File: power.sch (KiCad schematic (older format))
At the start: 30 parts, among them J11 Screw_Terminal_01x02, J2 BATT_OUT, J3 BATT_IN, K1 UMS05-1A80-75L, Q2 Q_NMOS_GSD, Q3 Q_NMOS_GSD, SW2 SW_Reed, U1 TPS3711, U5 P783F-Q24-S5-S

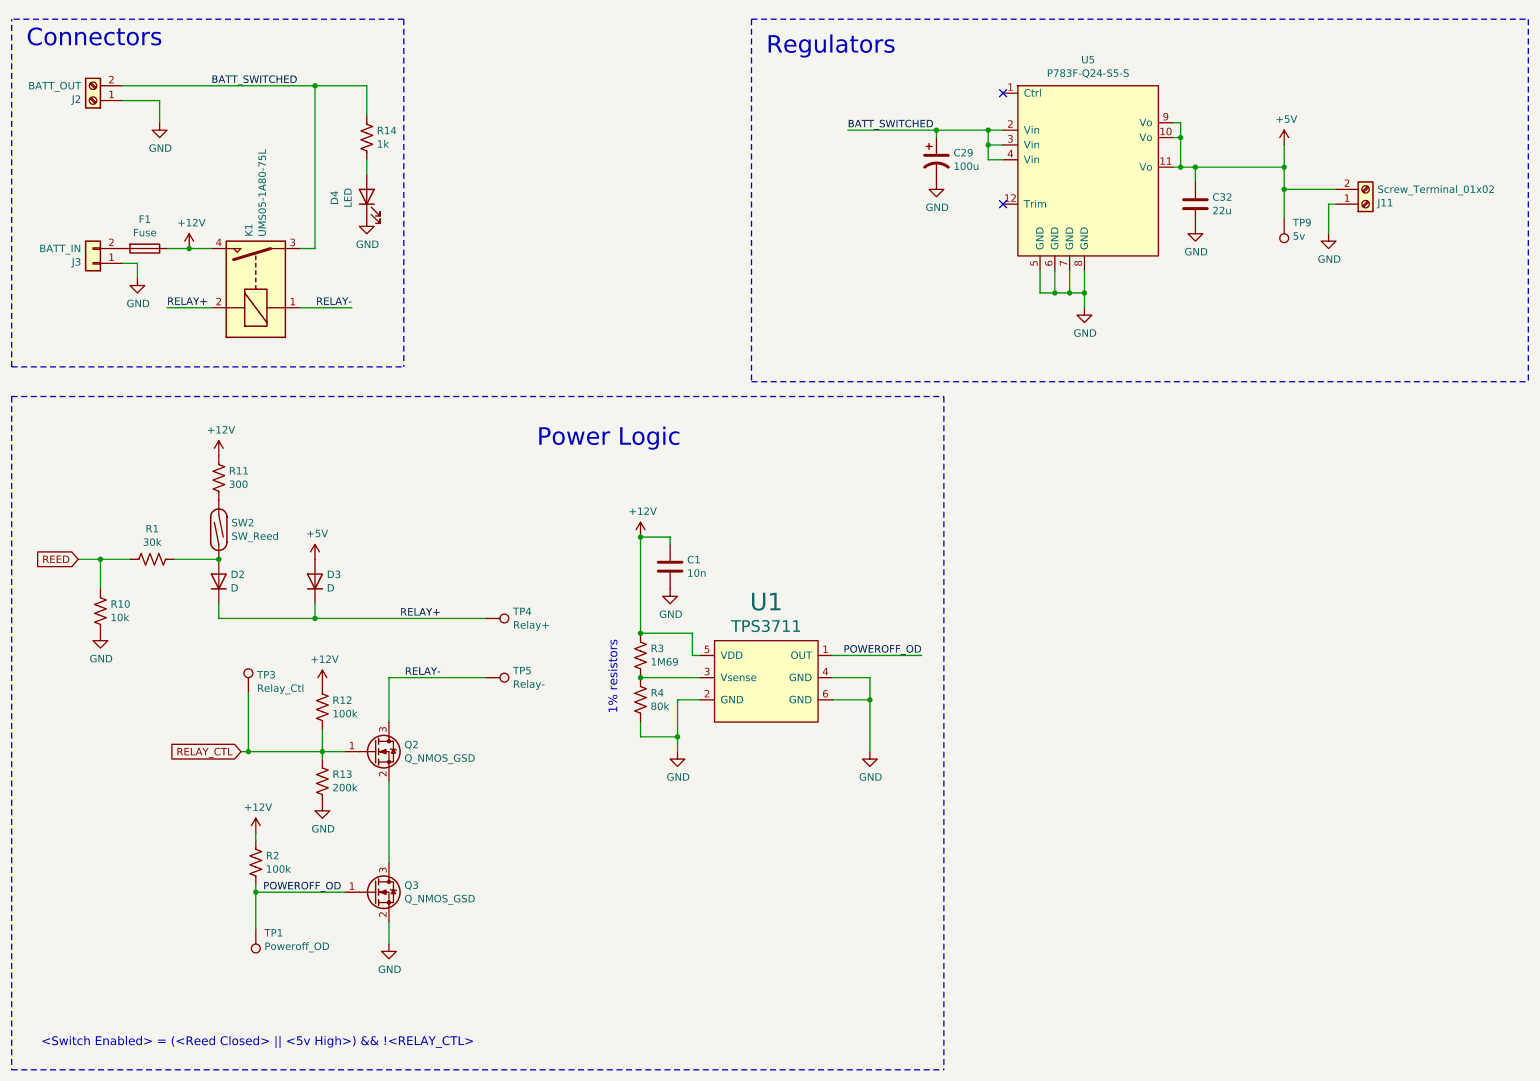
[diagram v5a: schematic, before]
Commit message: Revised for BlueRobotics switch.
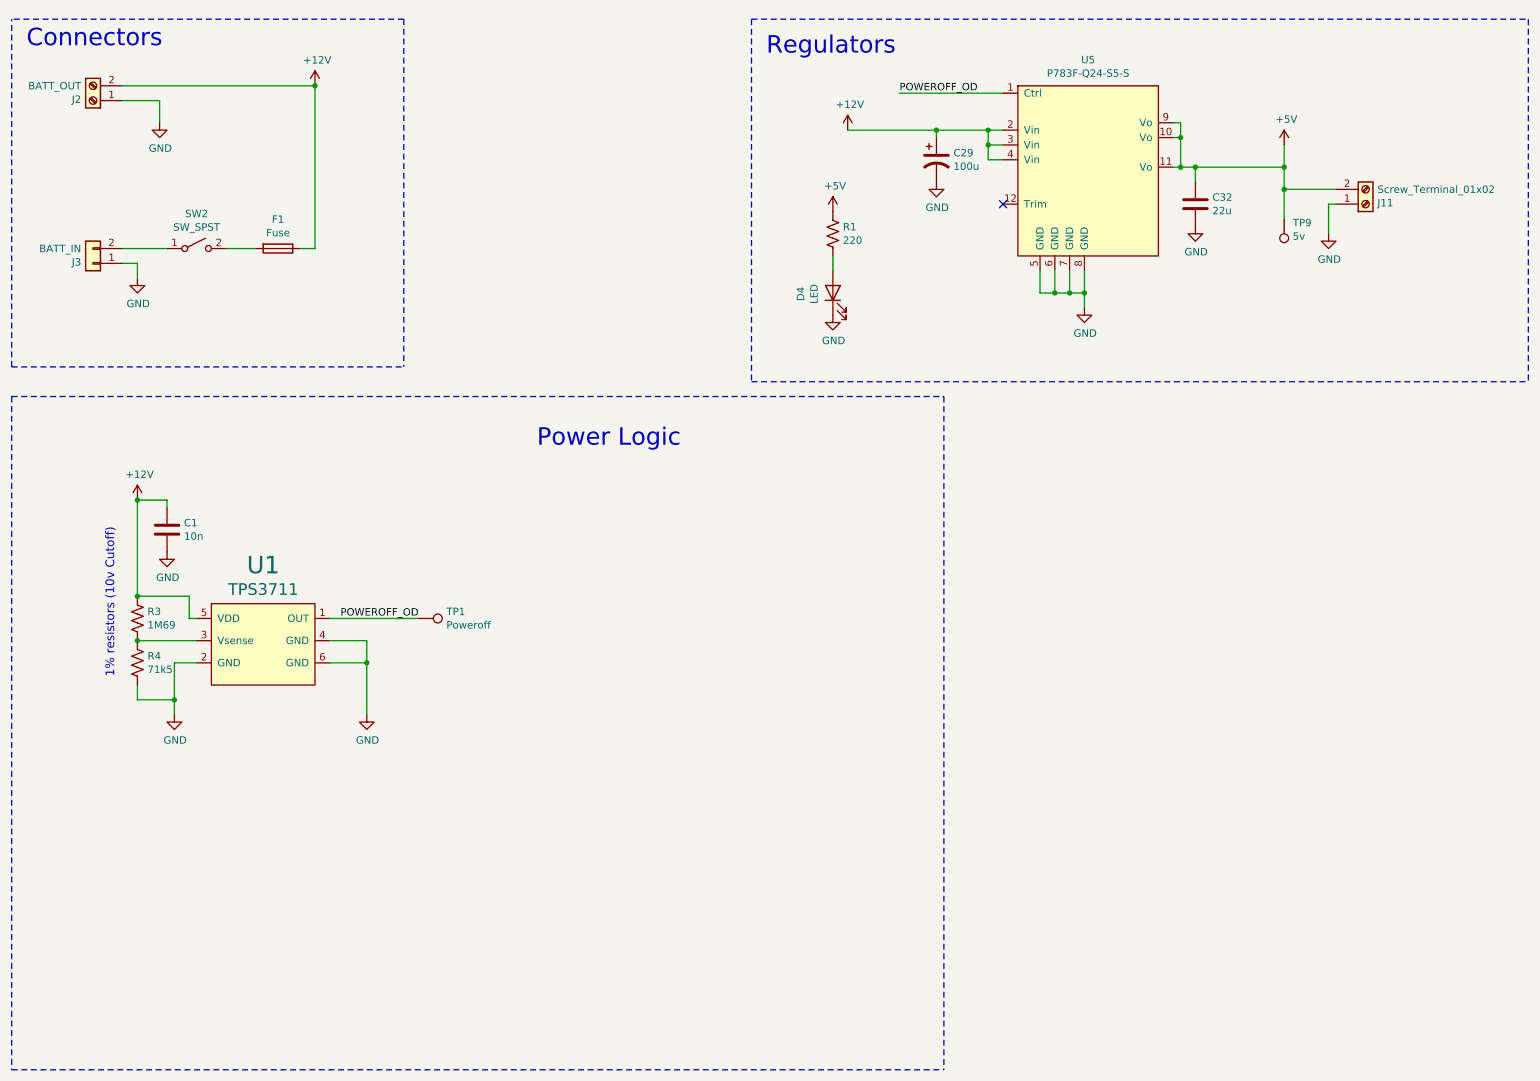
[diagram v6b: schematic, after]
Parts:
- removed D2, D3: D, Diode_SMD:D_1206_3216Metric_Pad1.42x1.75mm_HandSolder, symbol Device:D
- removed K1: UMS05-1A80-75L, Relay_THT:Relay_SPST_TE_PCN-1xxD3MHZ, symbol Relay:UMS05-1A80-75L
- removed Q2, Q3: Q_NMOS_GSD, Package_TO_SOT_SMD:SOT-23_Handsoldering, symbol Device:Q_NMOS_GSD
- removed R10: 10k, Resistor_SMD:R_1206_3216Metric_Pad1.30x1.75mm_HandSolder, symbol Device:R_US
- removed R11: 300, Resistor_SMD:R_1206_3216Metric_Pad1.30x1.75mm_HandSolder, symbol Device:R_US
- removed R12, R2: 100k, Resistor_SMD:R_1206_3216Metric_Pad1.30x1.75mm_HandSolder, symbol Device:R_US
- removed R13: 200k, Resistor_SMD:R_1206_3216Metric_Pad1.30x1.75mm_HandSolder, symbol Device:R_US
- removed R14: 1k, Resistor_SMD:R_1206_3216Metric_Pad1.30x1.75mm_HandSolder, symbol Device:R_US
- removed SW2: SW_Reed, Connector_JST:JST_PH_S2B-PH-K_1x02_P2.00mm_Horizontal, symbol Switch:SW_Reed
- removed TP3: Relay_Ctl, TestPoint:TestPoint_Pad_1.5x1.5mm, symbol Connector:TestPoint
- removed TP4: Relay+, TestPoint:TestPoint_Pad_1.5x1.5mm, symbol Connector:TestPoint
- removed TP5: Relay-, TestPoint:TestPoint_Pad_1.5x1.5mm, symbol Connector:TestPoint
- added SW2: SW_SPST, Connector_JST:JST_XH_S2B-XH-A_1x02_P2.50mm_Horizontal, symbol Switch:SW_SPST
- R1: value 30k -> 220
- R4: value 80k -> 71k5
- TP1: value Poweroff_OD -> Poweroff
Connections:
- net BATT_SWITCHED is gone; now on net +12V: C29.1, J2.2 (Pin_2), U5.2 (Vin), U5.3 (Vin), U5.4 (Vin)
- net REED is gone; now on an unnamed net: R1.2
- net +5V: now also R1.1
- net POWEROFF_OD: now also U5.1 (Ctrl)
- net at J3.2 (Pin_2): now also SW2.1 (A); no longer F1.2
- new net: F1.2, SW2.2 (B)
- no-connect marks 2 -> 1
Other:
- note added: "1% resistors (10v Cutoff)\n"
- note removed: "1% resistors\n"
- note removed: "<Switch Enabled> = (<Reed Closed> || <5v High>) && !<RELAY_CTL>"
- moved on the sheet: C1, D4, F1, R3, R4, U1

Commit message: Added load switch
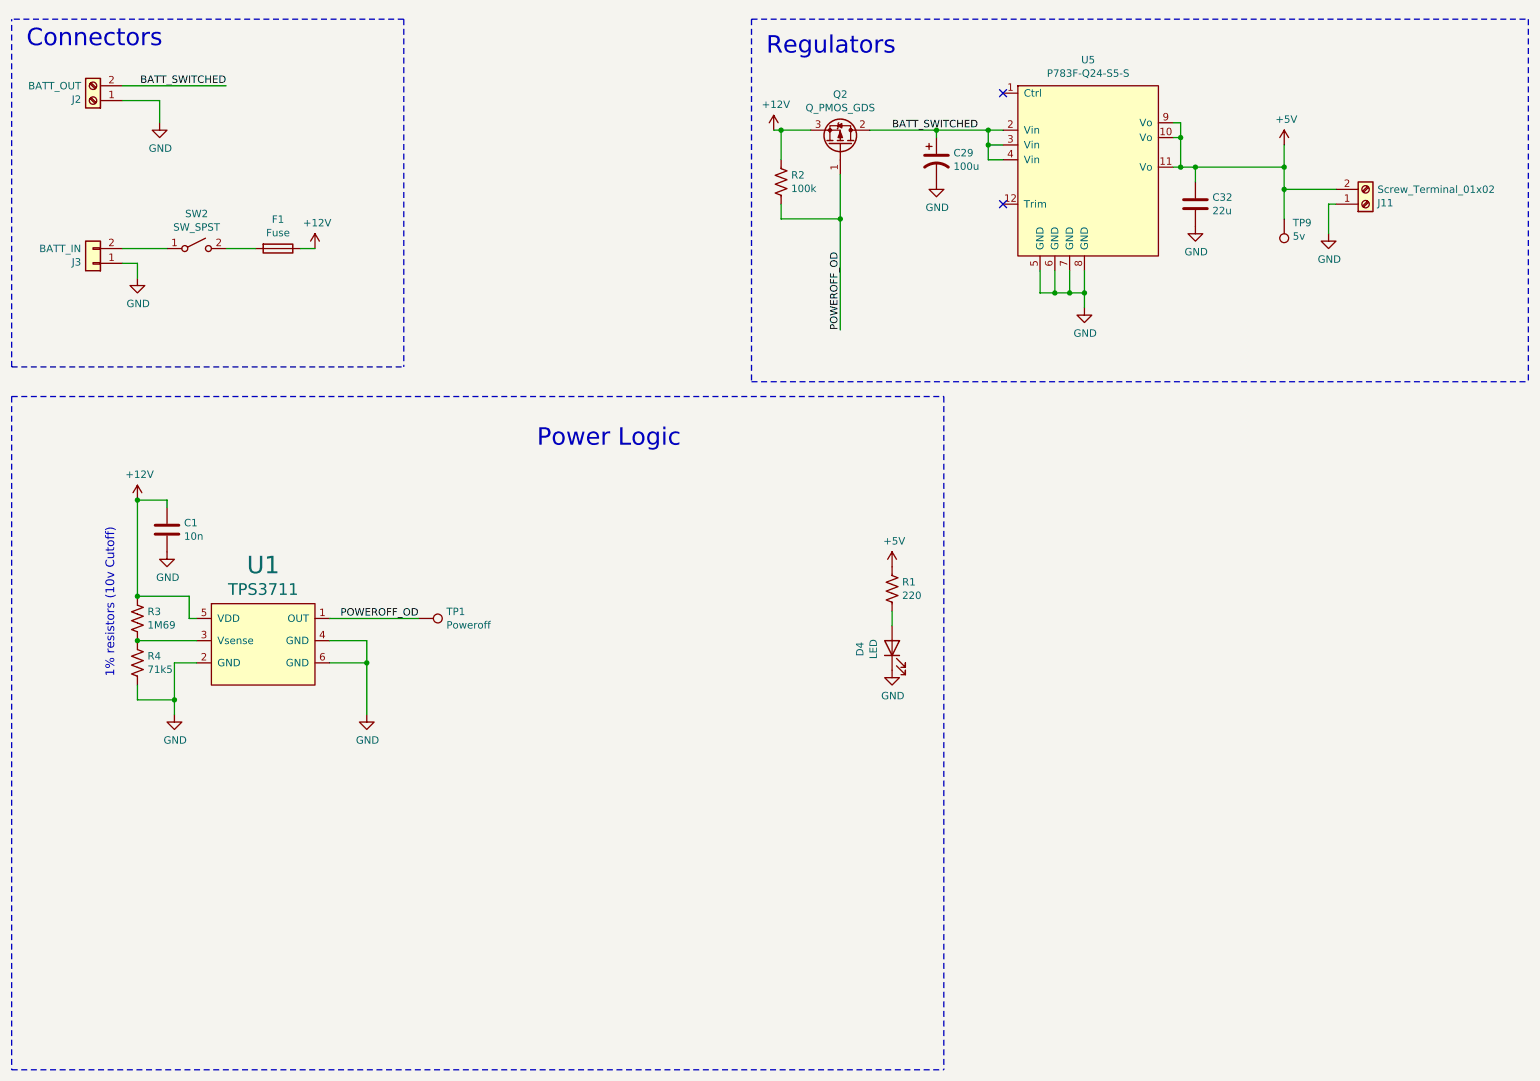
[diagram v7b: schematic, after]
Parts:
- added Q2: Q_PMOS_GDS, Package_TO_SOT_SMD:TO-252-2, symbol Device:Q_PMOS_GDS
- added R2: 100k, Resistor_SMD:R_1206_3216Metric_Pad1.30x1.75mm_HandSolder, symbol Device:R_US
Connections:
- net +12V: now also Q2.3 (S), R2.1; no longer C29.1, J2.2 (Pin_2), U5.2 (Vin), U5.3 (Vin), U5.4 (Vin)
- net POWEROFF_OD: now also Q2.1 (G), R2.2; no longer U5.1 (Ctrl)
- new net BATT_SWITCHED: C29.1, J2.2 (Pin_2), Q2.2 (D), U5.2 (Vin), U5.3 (Vin), U5.4 (Vin)
- no-connect marks 1 -> 2
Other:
- moved on the sheet: D4, R1
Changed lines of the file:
@@
 	1    0    0    -1
 $EndComp
-Wire Wire Line
-	6800 1350 6200 1350
-Connection ~ 6800 1350
 $Comp
 L power:GND #PWR0159
 U 1 1 617DE5F6
-P 6100 2600
-F 0 "#PWR0159" H 6100 2350 50  0001 C CNN
-F 1 "GND" H 6105 2427 50  0000 C CNN
-F 2 "" H 6100 2600 50  0001 C CNN
-F 3 "" H 6100 2600 50  0001 C CNN
-	1    6100 2600
+P 6500 5000
+F 0 "#PWR0159" H 6500 4750 50  0001 C CNN
+F 1 "GND" H 6505 4827 50  0000 C CNN
+F 2 "" H 6500 5000 50  0001 C CNN
+F 3 "" H 6500 5000 50  0001 C CNN
+	1    6500 5000
 	1    0    0    -1
 $EndComp
@@
 L Device:LED D4
 U 1 1 617BD1CA
-P 6100 2450
-F 0 "D4" H 6093 2667 50  0000 C CNN
-F 1 "LED" H 6093 2576 50  0000 C CNN
-F 2 "LED_THT:LED_D5.0mm_FlatTop" H 6100 2450 50  0001 C CNN
-F 3 "~" H 6100 2450 50  0001 C CNN
-	1    6100 2450
+P 6500 4850
+F 0 "D4" H 6493 5067 50  0000 C CNN
+F 1 "LED" H 6493 4976 50  0000 C CNN
+F 2 "LED_THT:LED_D5.0mm_FlatTop" H 6500 4850 50  0001 C CNN
+F 3 "~" H 6500 4850 50  0001 C CNN
+	1    6500 4850
 	0    -1   -1   0
 $EndComp
-Wire Wire Line
-	1300 1050 2600 1050
-Wire Wire Line
-	2600 1050 2600 2150
 Text Notes 650  800  0    118  ~ 0
 Connectors
@@
 Wire Notes Line width 20
 	550  3150 6850 3150
-Wire Wire Line
-	7250 1100 6550 1100
-Text Label 6550 1100 0    50   ~ 0
+Text Label 6150 2700 1    50   ~ 0
 POWEROFF_OD
 $Comp
@@
 L Device:R_US R1
 U 1 1 61B841FF
-P 6100 2050
-F 0 "R1" H 6168 2096 50  0000 L CNN
-F 1 "220" H 6168 2005 50  0000 L CNN
-F 2 "Resistor_SMD:R_1206_3216Metric_Pad1.30x1.75mm_HandSolder" V 6140 2040 50  0001 C CNN
-F 3 "~" H 6100 2050 50  0001 C CNN
-	1    6100 2050
-	1    0    0    -1
-$EndComp
-Wire Wire Line
-	6100 2200 6100 2300
+P 6500 4450
+F 0 "R1" H 6568 4496 50  0000 L CNN
+F 1 "220" H 6568 4405 50  0000 L CNN
+F 2 "Resistor_SMD:R_1206_3216Metric_Pad1.30x1.75mm_HandSolder" V 6540 4440 50  0001 C CNN
+F 3 "~" H 6500 4450 50  0001 C CNN
+	1    6500 4450
+	1    0    0    -1
+$EndComp
+Wire Wire Line
+	6500 4600 6500 4700
 $Comp
 L power:+5V #PWR0105
 U 1 1 61B85D82
-P 6100 1900
-F 0 "#PWR0105" H 6100 1750 50  0001 C CNN
-F 1 "+5V" H 6115 2073 50  0000 C CNN
-F 2 "" H 6100 1900 50  0001 C CNN
-F 3 "" H 6100 1900 50  0001 C CNN
-	1    6100 1900
+P 6500 4300
+F 0 "#PWR0105" H 6500 4150 50  0001 C CNN
+F 1 "+5V" H 6515 4473 50  0000 C CNN
+F 2 "" H 6500 4300 50  0001 C CNN
+F 3 "" H 6500 4300 50  0001 C CNN
+	1    6500 4300
 	1    0    0    -1
 $EndComp
@@
 L power:+12V #PWR0107
 U 1 1 61B965F1
-P 2600 1050
-F 0 "#PWR0107" H 2600 900 50  0001 C CNN
-F 1 "+12V" H 2615 1223 50  0000 C CNN
-F 2 "" H 2600 1050 50  0001 C CNN
-F 3 "" H 2600 1050 50  0001 C CNN
-	1    2600 1050
-	1    0    0    -1
-$EndComp
-Connection ~ 2600 1050
+P 2600 2150
+F 0 "#PWR0107" H 2600 2000 50  0001 C CNN
+F 1 "+12V" H 2615 2323 50  0000 C CNN
+F 2 "" H 2600 2150 50  0001 C CNN
+F 3 "" H 2600 2150 50  0001 C CNN
+	1    2600 2150
+	1    0    0    -1
+$EndComp
 $Comp
 L power:+12V #PWR0108
 U 1 1 61B99FD2
-P 6200 1350
-F 0 "#PWR0108" H 6200 1200 50  0001 C CNN
-F 1 "+12V" H 6215 1523 50  0000 C CNN
-F 2 "" H 6200 1350 50  0001 C CNN
-F 3 "" H 6200 1350 50  0001 C CNN
-	1    6200 1350
+P 5700 1350
+F 0 "#PWR0108" H 5700 1200 50  0001 C CNN
+F 1 "+12V" H 5715 1523 50  0000 C CNN
+F 2 "" H 5700 1350 50  0001 C CNN
+F 3 "" H 5700 1350 50  0001 C CNN
+	1    5700 1350
 	1    0    0    -1
 $EndComp
@@
 	0    1    1    0
 $EndComp
+NoConn ~ 7250 1100
+Wire Wire Line
+	5700 1350 5750 1350
+Wire Wire Line
+	6350 1350 6800 1350
+Connection ~ 6800 1350
+$Comp
+L Device:R_US R2
+U 1 1 61B4BEA5
+P 5750 1700
+F 0 "R2" H 5818 1746 50  0000 L CNN
+F 1 "100k" H 5818 1655 50  0000 L CNN
+F 2 "Resistor_SMD:R_1206_3216Metric_Pad1.30x1.75mm_HandSolder" V 5790 1690 50  0001 C CNN
+F 3 "~" H 5750 1700 50  0001 C CNN
+	1    5750 1700
+	1    0    0    -1
+$EndComp
+Wire Wire Line
+	5750 1550 5750 1350
+Connection ~ 5750 1350
+Wire Wire Line
+	5750 1350 5950 1350
+Wire Wire Line
+	5750 1850 5750 1950
+Wire Wire Line
+	5750 1950 6150 1950
+Wire Wire Line
+	6150 1950 6150 2700
+Wire Wire Line
+	6150 1950 6150 1650
+Connection ~ 6150 1950
+$Comp
+L Device:Q_PMOS_GDS Q2
+U 1 1 61B57A2C
+P 6150 1450
+F 0 "Q2" V 6492 1450 50  0000 C CNN
+F 1 "Q_PMOS_GDS" V 6401 1450 50  0000 C CNN
+F 2 "Package_TO_SOT_SMD:TO-252-2" H 6350 1550 50  0001 C CNN
+F 3 "~" H 6150 1450 50  0001 C CNN
+	1    6150 1450
+	0    1    -1   0
+$EndComp
+Text Label 6500 1350 0    50   ~ 0
+BATT_SWITCHED
+Wire Wire Line
+	1300 1050 2000 1050
+Text Label 2000 1050 2    50   ~ 0
+BATT_SWITCHED
 $EndSCHEMATC

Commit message: Some footprint and part changes based on availability.
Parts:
- C32: footprint Capacitor_SMD:C_1206_3216Metric -> Capacitor_SMD:C_1206_3216Metric_Pad1.33x1.80mm_HandSolder
- Q2: footprint Package_TO_SOT_SMD:TO-252-2 -> Package_TO_SOT_THT:TO-251-3_Vertical
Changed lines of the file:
@@
 F 0 "C32" H 8665 1896 50  0000 L CNN
 F 1 "22u" H 8665 1805 50  0000 L CNN
-F 2 "Capacitor_SMD:C_1206_3216Metric" H 8588 1700 50  0001 C CNN
+F 2 "Capacitor_SMD:C_1206_3216Metric_Pad1.33x1.80mm_HandSolder" H 8588 1700 50  0001 C CNN
 F 3 "~" H 8550 1850 50  0001 C CNN
 	1    8550 1850
@@
 F 0 "Q2" V 6492 1450 50  0000 C CNN
 F 1 "Q_PMOS_GDS" V 6401 1450 50  0000 C CNN
-F 2 "Package_TO_SOT_SMD:TO-252-2" H 6350 1550 50  0001 C CNN
+F 2 "Package_TO_SOT_THT:TO-251-3_Vertical" H 6350 1550 50  0001 C CNN
 F 3 "~" H 6150 1450 50  0001 C CNN
 	1    6150 1450
